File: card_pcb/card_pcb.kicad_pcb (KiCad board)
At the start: 2 copper layers, 85 x 54 mm, 44 parts

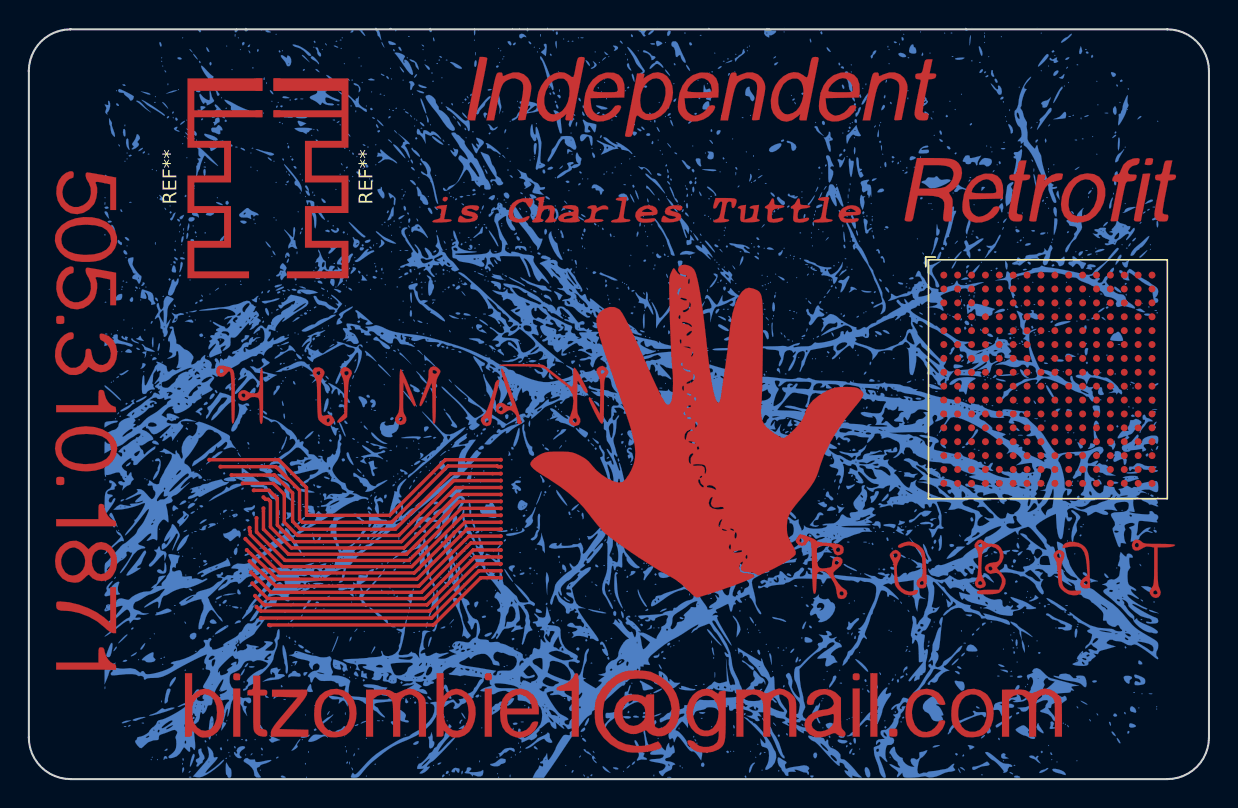
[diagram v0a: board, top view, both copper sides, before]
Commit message: a trim off the top
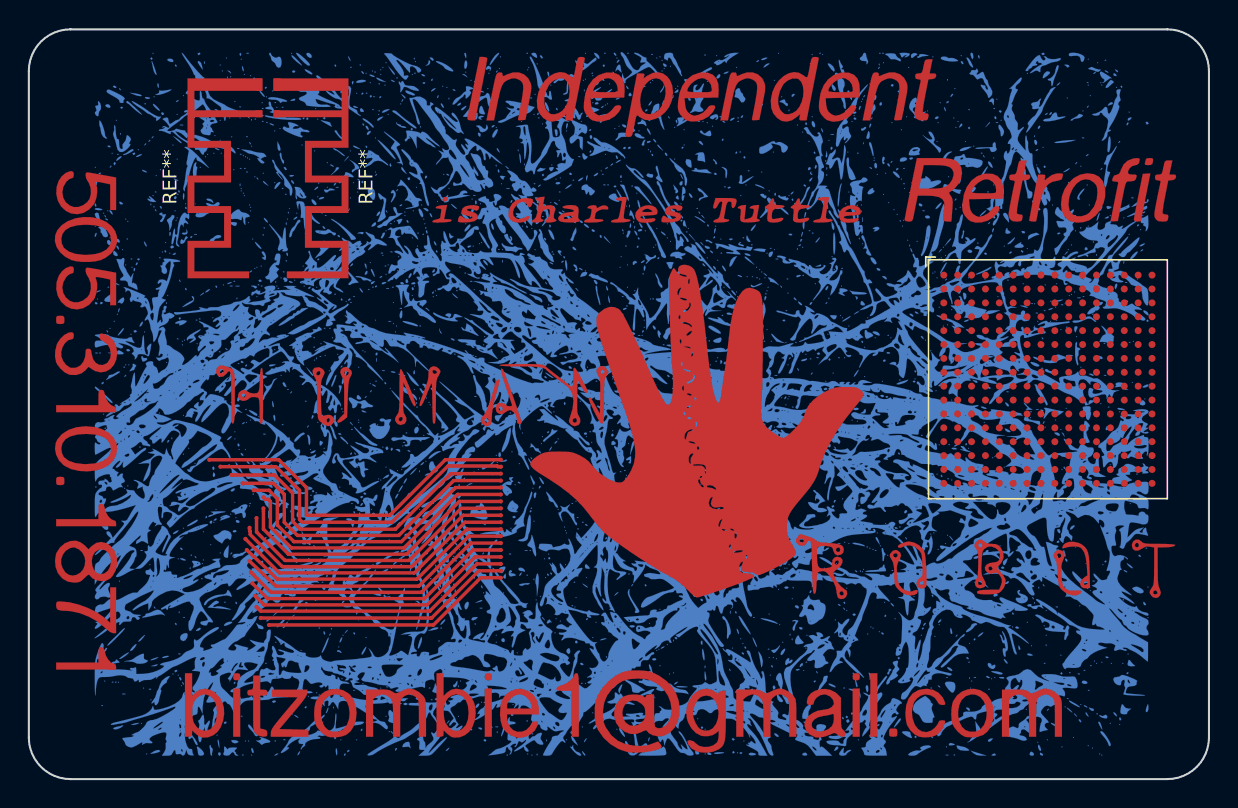
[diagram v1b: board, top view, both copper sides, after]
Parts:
- removed G5: LOGO, mylogos:fungi_2
- added G***: LOGO, mylogos:fungi_2_trim, B.Cu at (113.7, 62.0)
